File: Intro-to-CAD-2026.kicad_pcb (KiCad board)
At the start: 4 copper layers, 100 x 100 mm, 215 parts, among them J1 ADC IN, J10 Conn_01x20_Socket, J11 SDR ANT, J12 SDR Out, J2 Conn_02x20_Counter_Clockwise, J3 Conn_02x20_Counter_Clockwise, J4 Conn_01x20_Socket, J5 +12V, J7 Conn_01x01_Pin, J8 OSC OUT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

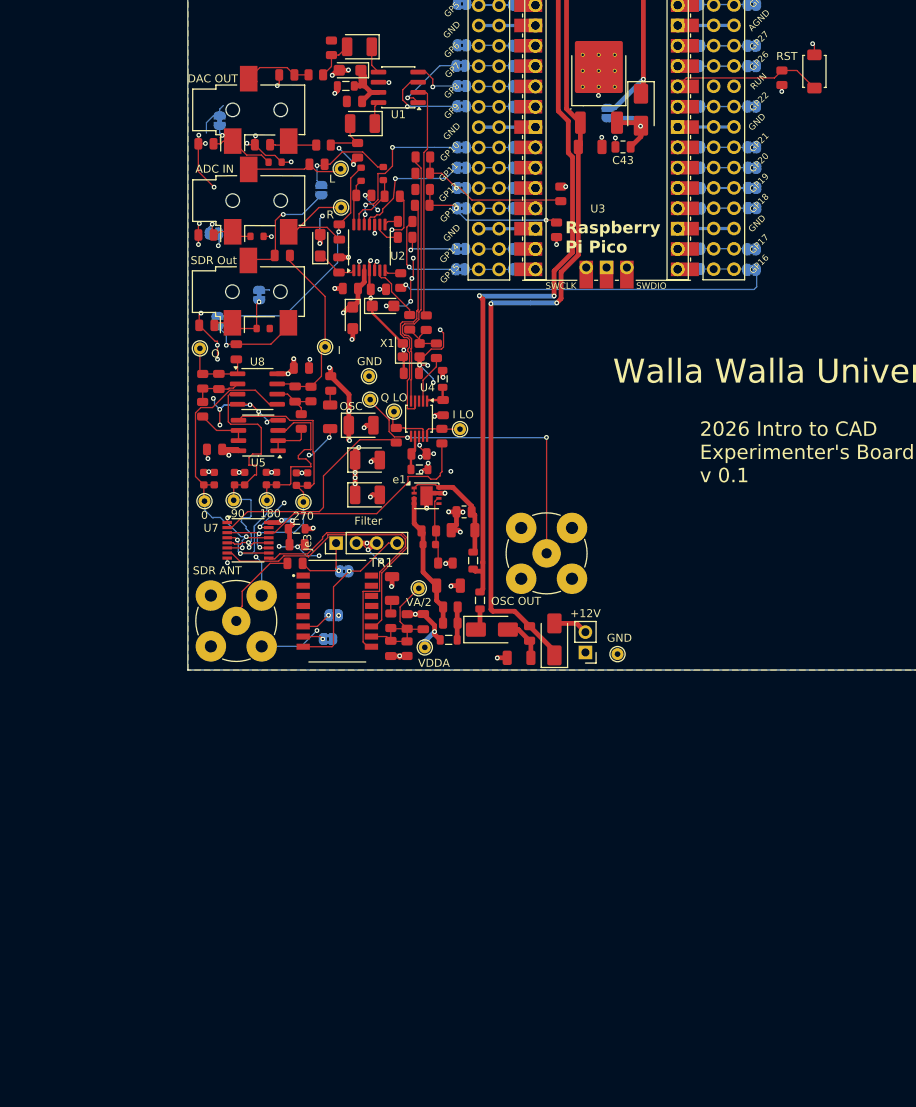
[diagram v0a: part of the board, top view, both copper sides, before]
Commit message: Changed C_sample to 10nf
And added 10 Ohm damping resistors.
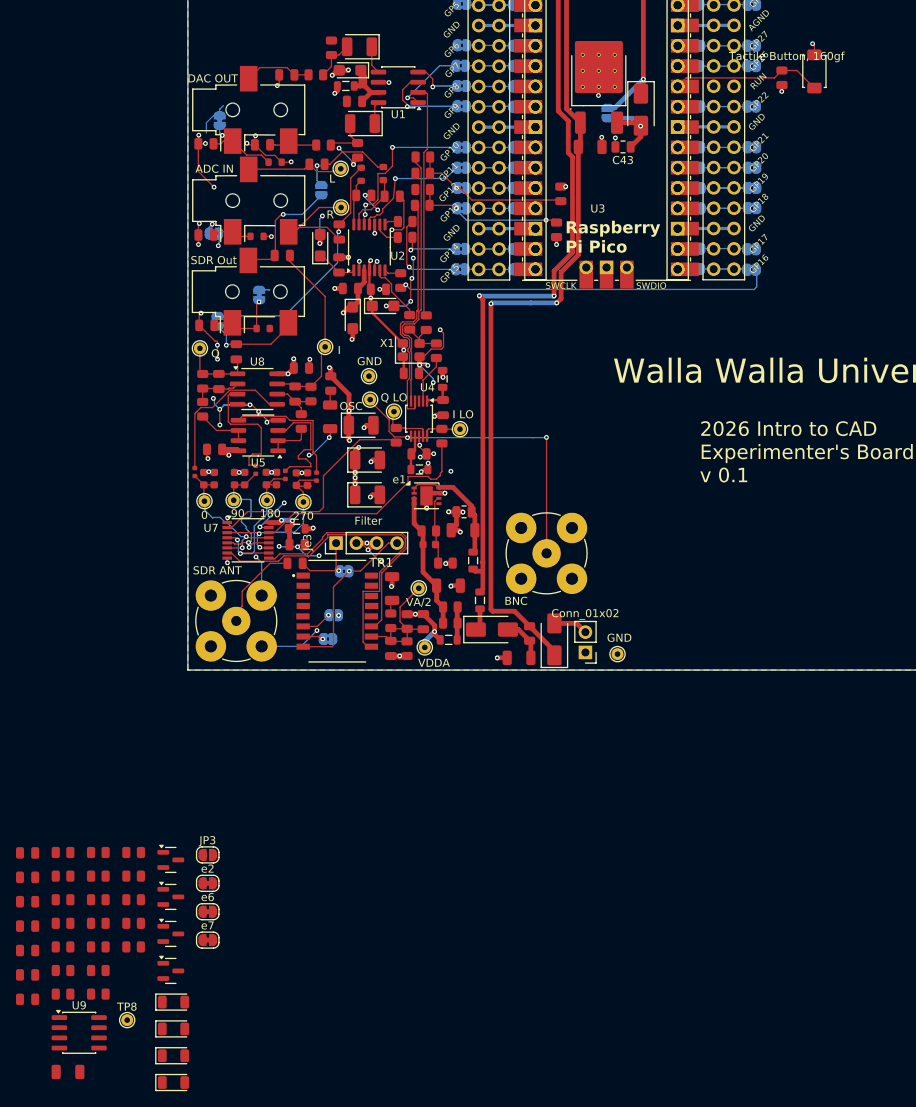
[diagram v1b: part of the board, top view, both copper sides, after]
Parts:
- added C54: 10uF, PCM_JLCPCB:C_1206, F.Cu at (86.0, 181.2)
- added C56: 100nF, PCM_JLCPCB:C_0805, F.Cu at (80.9, 153.8)
- added C57: 10uF, PCM_JLCPCB:C_0805, F.Cu at (80.9, 156.9)
- added C58: 10uF, PCM_JLCPCB:C_0805, F.Cu at (80.9, 159.9)
- added C59: 10uF, PCM_JLCPCB:C_0805, F.Cu at (80.9, 163.0)
- added C60: 10uF, PCM_JLCPCB:C_0805, F.Cu at (80.9, 166.0)
- added C61: 100nF, PCM_JLCPCB:C_0805, F.Cu at (80.9, 169.1)
- added C63: 10uF, PCM_JLCPCB:C_0805, F.Cu at (80.9, 172.1)
- added D4: SM4007PL, PCM_JLCPCB:D_SOD-123FL, F.Cu at (99.2, 172.5)
- added D5: SM4007PL, PCM_JLCPCB:D_SOD-123FL, F.Cu at (99.2, 175.8)
- added D6: SM4007PL, PCM_JLCPCB:D_SOD-123FL, F.Cu at (99.2, 179.2)
- added D7: SM4007PL, PCM_JLCPCB:D_SOD-123FL, F.Cu at (99.2, 182.5)
- added JP3: ~, Jumper:SolderJumper-2_P1.3mm_Open_RoundedPad1.0x1.5mm, F.Cu at (103.4, 154.1)
- added Q2: FMMT591, PCM_JLCPCB:Q_SOT-23, F.Cu at (98.8, 154.7)
- added Q3: FMMT491, PCM_JLCPCB:Q_SOT-23, F.Cu at (98.8, 159.3)
- added Q4: FMMT491, PCM_JLCPCB:Q_SOT-23, F.Cu at (98.8, 163.9)
- added Q5: FMMT591, PCM_JLCPCB:Q_SOT-23, F.Cu at (98.8, 168.6)
- added R39: 1Ω, PCM_JLCPCB:R_0805, F.Cu at (85.3, 153.8)
- added R40: 1Ω, PCM_JLCPCB:R_0805, F.Cu at (85.3, 156.7)
- added R41: 1Ω, PCM_JLCPCB:R_0805, F.Cu at (85.3, 159.7)
- added R42: 1.5kΩ, PCM_JLCPCB:R_0805, F.Cu at (85.3, 162.6)
- added R43: 1.5kΩ, PCM_JLCPCB:R_0805, F.Cu at (85.3, 165.6)
- added R44: 1kΩ, PCM_JLCPCB:R_0805, F.Cu at (85.3, 168.5)
- added R45: 10kΩ, PCM_JLCPCB:R_0805, F.Cu at (85.3, 171.5)
- added R46: 1.5kΩ, PCM_JLCPCB:R_0805, F.Cu at (89.8, 153.8)
- added R47: 1.5kΩ, PCM_JLCPCB:R_0805, F.Cu at (89.8, 156.7)
- added R48: 1Ω, PCM_JLCPCB:R_0805, F.Cu at (89.8, 159.7)
- added R49: 1Ω, PCM_JLCPCB:R_0805, F.Cu at (89.8, 162.6)
- added R50: 10kΩ, PCM_JLCPCB:R_0805, F.Cu at (89.8, 165.6)
- added R51: 10kΩ, PCM_JLCPCB:R_0805, F.Cu at (89.8, 168.5)
- added R52: 2.2kΩ, PCM_JLCPCB:R_0805, F.Cu at (89.8, 171.5)
- added R53: 2.2kΩ, PCM_JLCPCB:R_0805, F.Cu at (94.2, 153.8)
- added R54: 100Ω, PCM_JLCPCB:R_0805, F.Cu at (94.2, 156.7)
- added R55: 100Ω, PCM_JLCPCB:R_0805, F.Cu at (94.2, 159.7)
- added R56: 100Ω, PCM_JLCPCB:R_0805, F.Cu at (94.2, 162.6)
- added R57: 100Ω, PCM_JLCPCB:R_0805, F.Cu at (94.2, 165.6)
- added R58: 10Ω, PCM_JLCPCB:R_0402, F.Cu at (117.0, 106.8)
- added R59: 10Ω, PCM_JLCPCB:R_0402, F.Cu at (109.4, 105.9)
- added R60: 10Ω, PCM_JLCPCB:R_0402, F.Cu at (101.8, 106.2)
- added R61: 10Ω, PCM_JLCPCB:R_0402, F.Cu at (113.1, 106.6)
- added TP8: V_R, TestPoint:TestPoint_THTPad_D1.5mm_Drill0.7mm, F.Cu at (93.4, 174.7)
- added U9: OPA1612AxD, Package_SO:SOIC-8_3.9x4.9mm_P1.27mm, F.Cu at (87.4, 176.3)
- added e2: ~, Jumper:SolderJumper-2_P1.3mm_Bridged_RoundedPad1.0x1.5mm, F.Cu at (103.4, 157.6)
- added e6: ~, Jumper:SolderJumper-2_P1.3mm_Bridged_RoundedPad1.0x1.5mm, F.Cu at (103.4, 161.2)
- added e7: ~, Jumper:SolderJumper-2_P1.3mm_Bridged_RoundedPad1.0x1.5mm, F.Cu at (103.4, 164.7)
- C14, C16, C19, C22, C24, C25, C26, C27: value 330pF -> 10nF
- J5: value +12V -> Conn_01x02
- J8: value OSC OUT -> BNC
- S1: value RST -> Tactile Button, 160gf
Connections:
- net Net-(Q1-G) renamed VAH
- C14 pad 1: Net-(U7-1B1) -> Net-(U7-1B2)
- C19 pad 1: Net-(U7-1B2) -> Net-(U7-1B3)
- C22 pad 1: Net-(U5A-+) -> Net-(U7-1B4)
- C24 pad 1: Net-(U5B-+) -> Net-(U7-1B1)
- C26 pad 1: Net-(U5A-+) -> Net-(U7-1B3)
- C27 pad 1: Net-(U5B-+) -> Net-(U7-1B4)
- C49 pad 1: Net-(C49-Pad1) -> Net-(e6-A)
- C53 pad 1: Net-(C53-Pad1) -> Net-(e7-B)
- J9 pad R: Net-(C49-Pad1) -> Net-(C59-Pad2)
- J9 pad T: Net-(C53-Pad1) -> Net-(C60-Pad2)
- R22 pad 2: Net-(C49-Pad1) -> Net-(e6-A)
- R33 pad 2: Net-(C53-Pad1) -> Net-(e7-B)
- TP6 pad 1: Net-(U5A-+) -> Net-(U7-1B3)
- TP7 pad 1: Net-(U5B-+) -> Net-(U7-1B4)
- U7 pad 10: Net-(U5A-+) -> Net-(U7-1B3)
- U7 pad 11: Net-(U5B-+) -> Net-(U7-1B4)
- U7 pad 3: Net-(U5B-+) -> Net-(U7-1B4)
- U7 pad 4: Net-(U5A-+) -> Net-(U7-1B3)
- U8 pad 3: Net-(U7-1B2) -> Net-(U8A-+)
- U8 pad 5: Net-(U7-1B1) -> Net-(U8B-+)
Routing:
- net Net-(U7-1B1): track 39.0 -> 18.9 mm
- net Net-(U8B-+): track 0.00 -> 19.3 mm
- net Net-(U7-1B2): track 37.8 -> 20.7 mm
- net Net-(U8A-+): track 0.00 -> 15.9 mm
- net (no net): track 0.00 -> 14.7 mm
- net Net-(C49-Pad1): track 8.88 -> 0.00 mm
- net Net-(C53-Pad1): track 5.79 -> 0.00 mm
- net Net-(U5A-+): track 38.5 -> 35.4 mm
- net Net-(U7-1B4): track 0.00 -> 2.70 mm
- net Net-(U7-1B3): track 0.00 -> 2.57 mm
- net Net-(U5B-+): track 38.4 -> 36.8 mm
- net unconnected-(U3-SWCLK-Pad41)_1: track 0.52 -> 0.00 mm
- net unconnected-(U3-SWCLK-Pad41): track 0.00 -> 0.52 mm

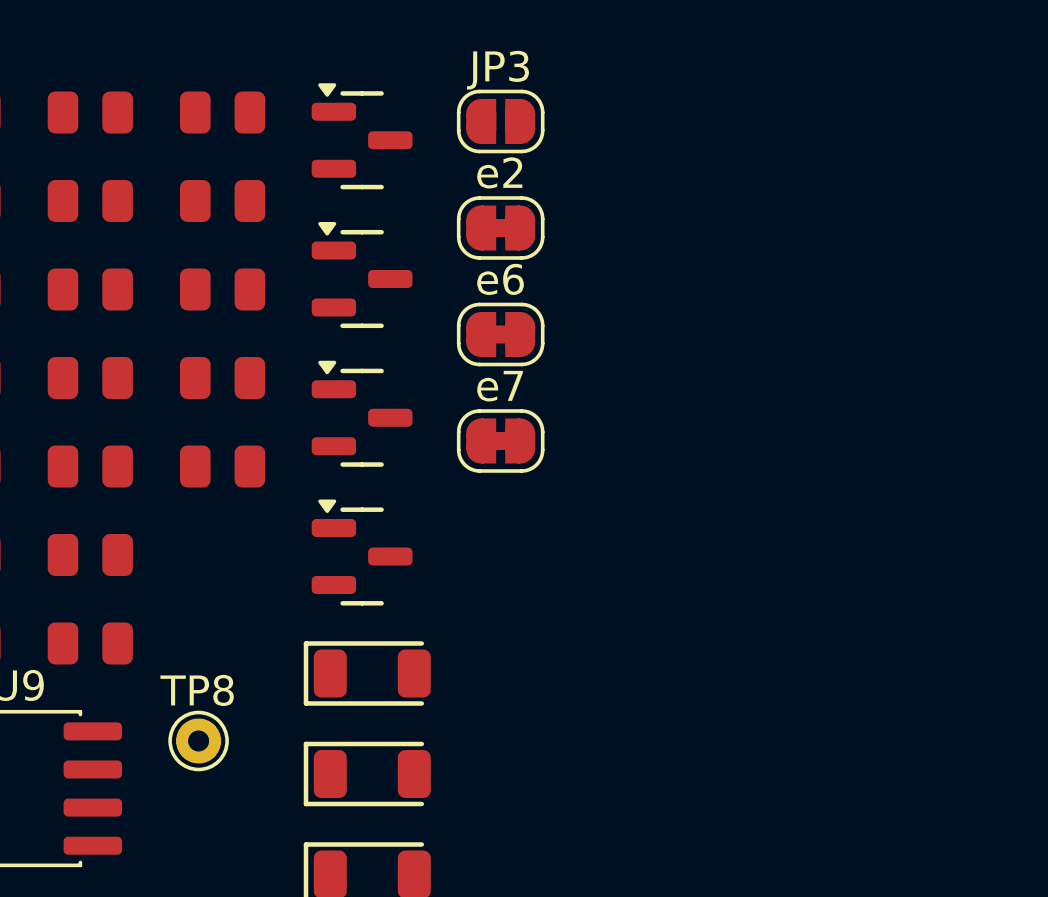
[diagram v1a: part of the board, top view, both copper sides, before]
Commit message: Changed R55-58 values.
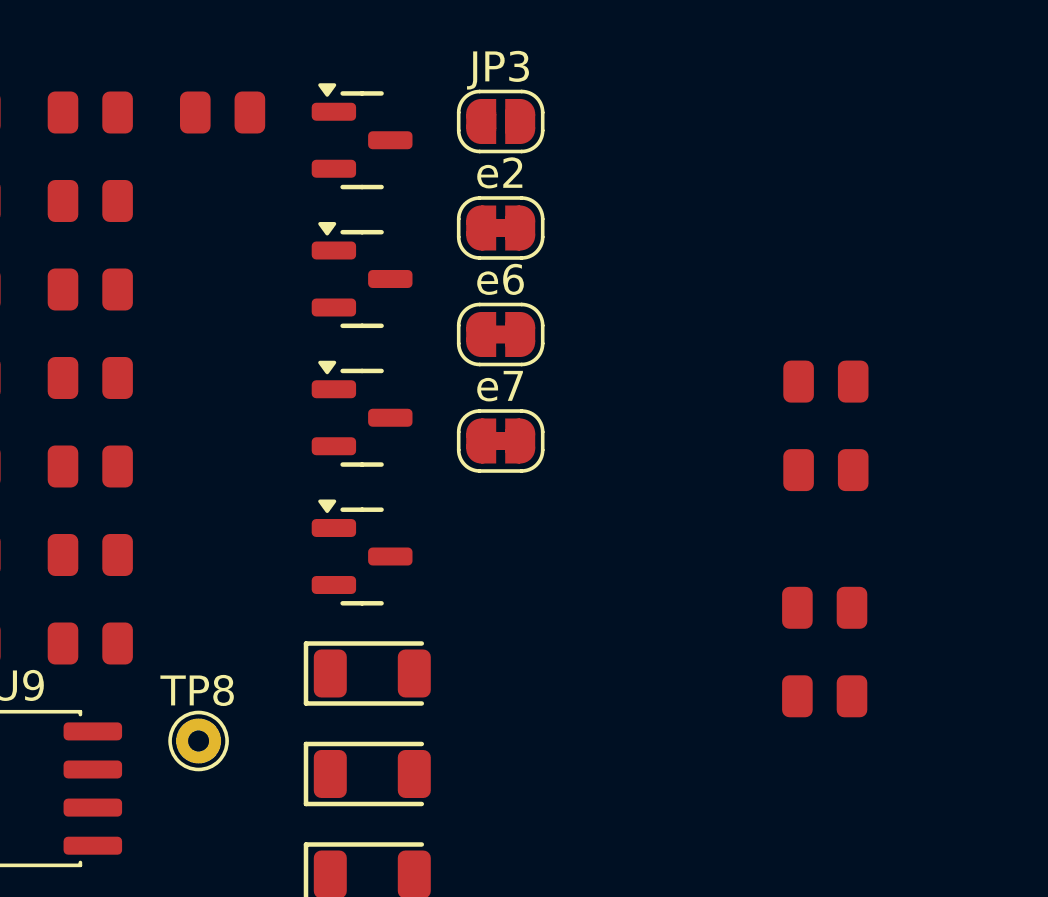
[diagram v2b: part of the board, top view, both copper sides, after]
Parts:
- removed R57: 100Ω, PCM_JLCPCB:R_0805
- added R62: 27Ω, PCM_JLCPCB:R_0805, F.Cu at (114.3, 165.7)
- R54, R55, R56: value 100Ω -> 27Ω
- moved R54 24.2 mm to (114.2, 170.3)
- moved R56 22.7 mm to (114.2, 173.2)
- moved R55 20.3 mm to (114.3, 162.7)
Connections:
- R54 pad 1: Net-(R54-Pad1) -> Net-(D6-Pad1)
- R54 pad 2: Net-(D5-Pad2) -> Net-(R54-Pad2)
- R55 pad 2: Net-(R54-Pad1) -> Net-(R55-Pad2)
- R56 pad 1: Net-(D6-Pad1) -> Net-(R54-Pad2)
- R56 pad 2: Net-(R56-Pad2) -> Net-(D7-Pad2)
- TR1 pad 12: (no net) -> unconnected-(TR1-Pad12)
- TR1 pad 13: (no net) -> unconnected-(TR1-Pad13)
- TR1 pad 4: (no net) -> unconnected-(TR1-Pad4)
- TR1 pad 5: (no net) -> unconnected-(TR1-Pad5)
- U9 pad 1: Net-(R54-Pad1) -> Net-(R55-Pad2)
- U9 pad 7: Net-(R56-Pad2) -> Net-(R54-Pad2)

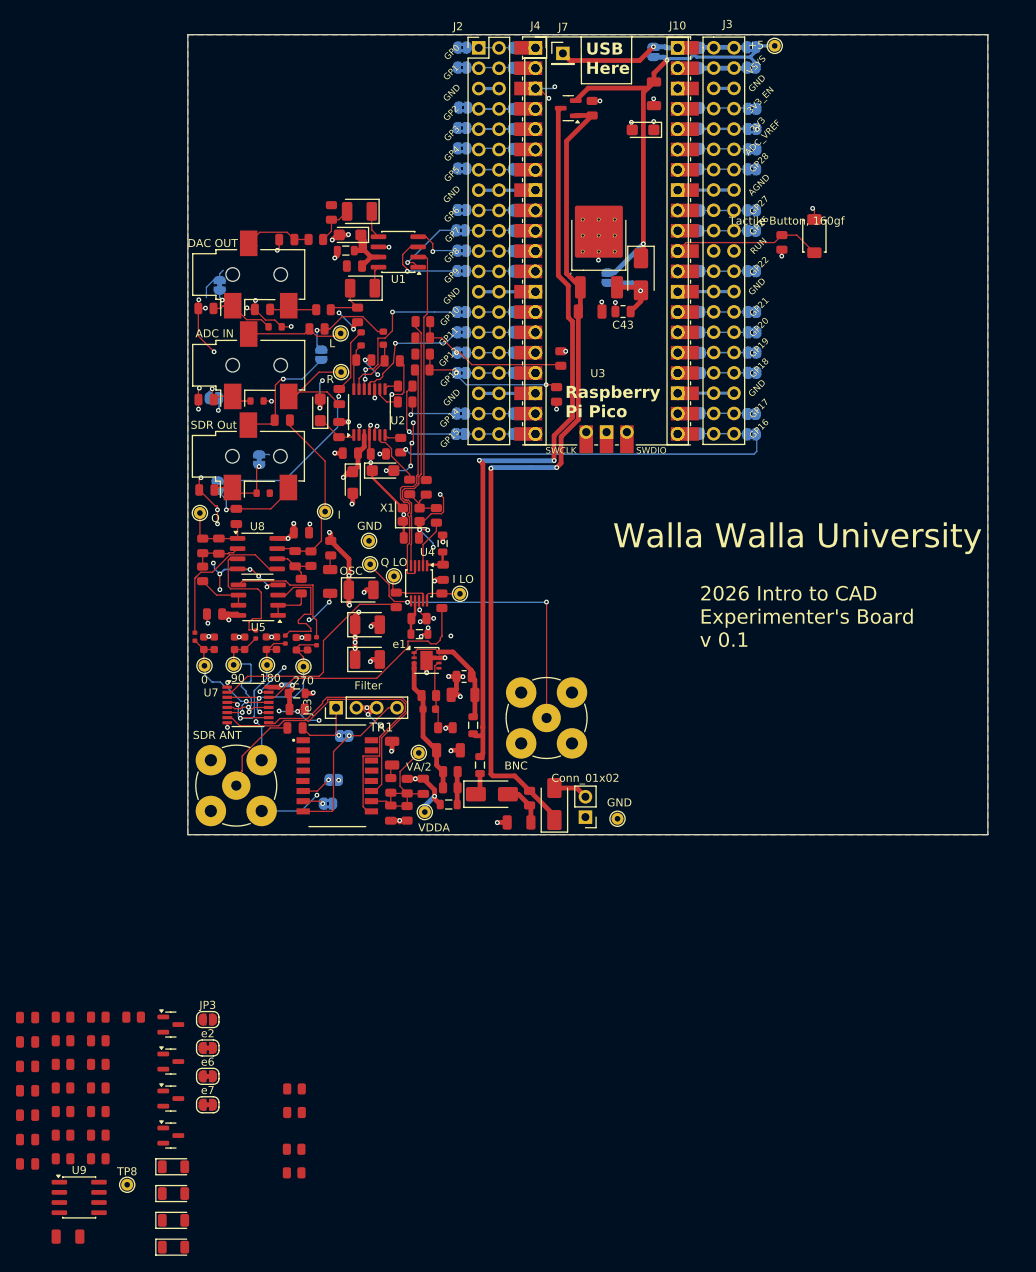
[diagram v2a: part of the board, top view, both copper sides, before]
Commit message: Moved DAC jack and planes.
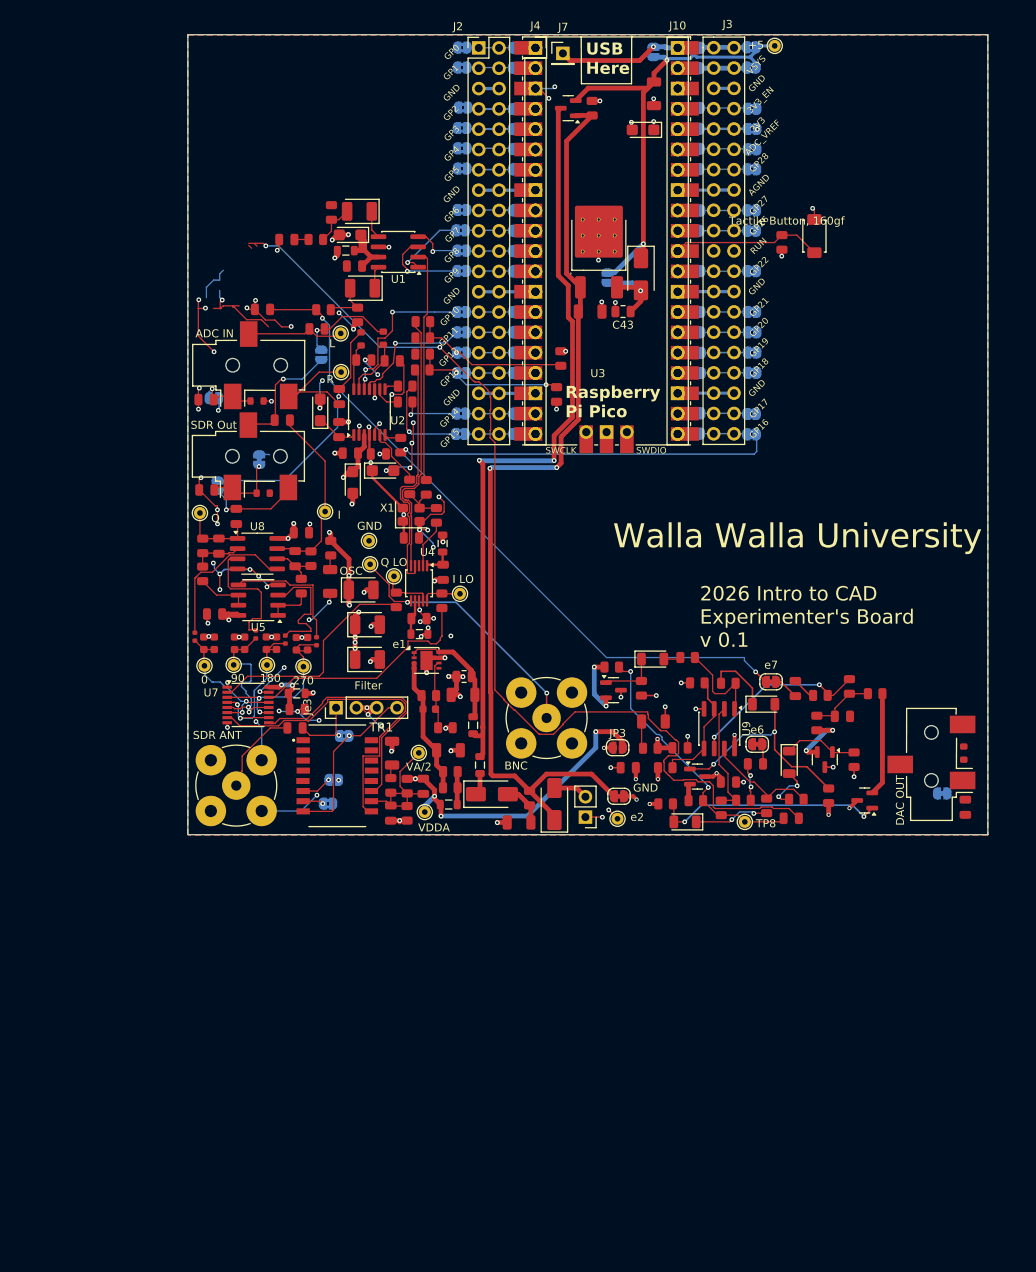
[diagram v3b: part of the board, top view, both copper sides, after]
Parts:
- moved C50 113.6 mm to (198.1, 127.5), turned to 90 degrees
- moved C60 113.4 mm to (182.8, 116.2)
- moved e3 110.4 mm to (195.2, 125.8), turned to 0 degrees
- moved R50 107.9 mm to (183.7, 112.4), turned to -90 degrees
- moved R48 107.6 mm to (186.9, 113.3)
- moved C58 107.0 mm to (176.9, 112.7), turned to 90 degrees
- moved R51 105.7 mm to (180.0, 113.5)
- moved R42 102.4 mm to (181.1, 126.1), turned to 90 degrees
- moved J9 102.2 mm to (193.9, 120.2), turned to 180 degrees
- moved C59 101.3 mm to (176.4, 128.9)
- moved R19 101.2 mm to (197.9, 120.8), turned to 90 degrees
- moved R47 100.8 mm to (184.2, 121.6), turned to -90 degrees
- moved R49 100.7 mm to (179.6, 117.0), turned to 90 degrees
- moved U9 99.2 mm to (167.4, 117.7), turned to -90 degrees
- moved C61 98.3 mm to (168.5, 124.4)
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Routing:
- net Net-(C59-Pad2): track 0.00 -> 131.0 mm, vias 0 -> 2
- net Net-(e7-B): track 0.00 -> 85.4 mm, vias 0 -> 2
- net Net-(C59-Pad1): track 0.00 -> 33.7 mm, vias 0 -> 2
- net VDDA: track 39.3 -> 70.3 mm, vias 14 -> 16
- net Net-(Q4-B): track 0.00 -> 29.0 mm, vias 0 -> 2
- net Net-(Q3-B): track 0.00 -> 27.0 mm, vias 0 -> 2
- net Net-(U9B--): track 0.00 -> 22.7 mm, vias 0 -> 2
- net GND: track 243.2 -> 263.1 mm, vias 92 -> 104
- net VAO: track 0.00 -> 17.4 mm, vias 0 -> 10
- net /DAC/VA/2: track 0.00 -> 14.8 mm
- net (no net): track 14.7 -> 0.00 mm
- net Net-(U9A--): track 0.00 -> 14.5 mm
- net Net-(R54-Pad2): track 0.00 -> 14.4 mm
- net Net-(Q4-E): track 0.00 -> 12.9 mm
- net VAH: track 106.5 -> 119.2 mm
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- added copper zone on In2.Cu, net VAO

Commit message: Save to go home.
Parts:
- moved C53 4.05 mm to (114.3, 65.5)
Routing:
- net GND: track 263.1 -> 242.4 mm, vias 104 -> 98
- net Net-(e3-B): track 11.8 -> 0.00 mm, vias 1 -> 0
- net Net-(e7-B): track 85.4 -> 79.6 mm
- net Net-(C59-Pad2): track 131.0 -> 126.2 mm, vias 2 -> 1
